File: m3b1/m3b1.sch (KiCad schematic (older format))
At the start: 26 parts, among them P5 MicroD-37Pins, Q1 MD3251, Q2 MD3251, U1 MC307, U10 MC309, U11 MC309, U12 MC310, U13 MC309, U2 MC306, U3 MC306, U4 MC306, U5 MC302, U6 MC306, U7 MC306, U8 MC301, U9 MC301

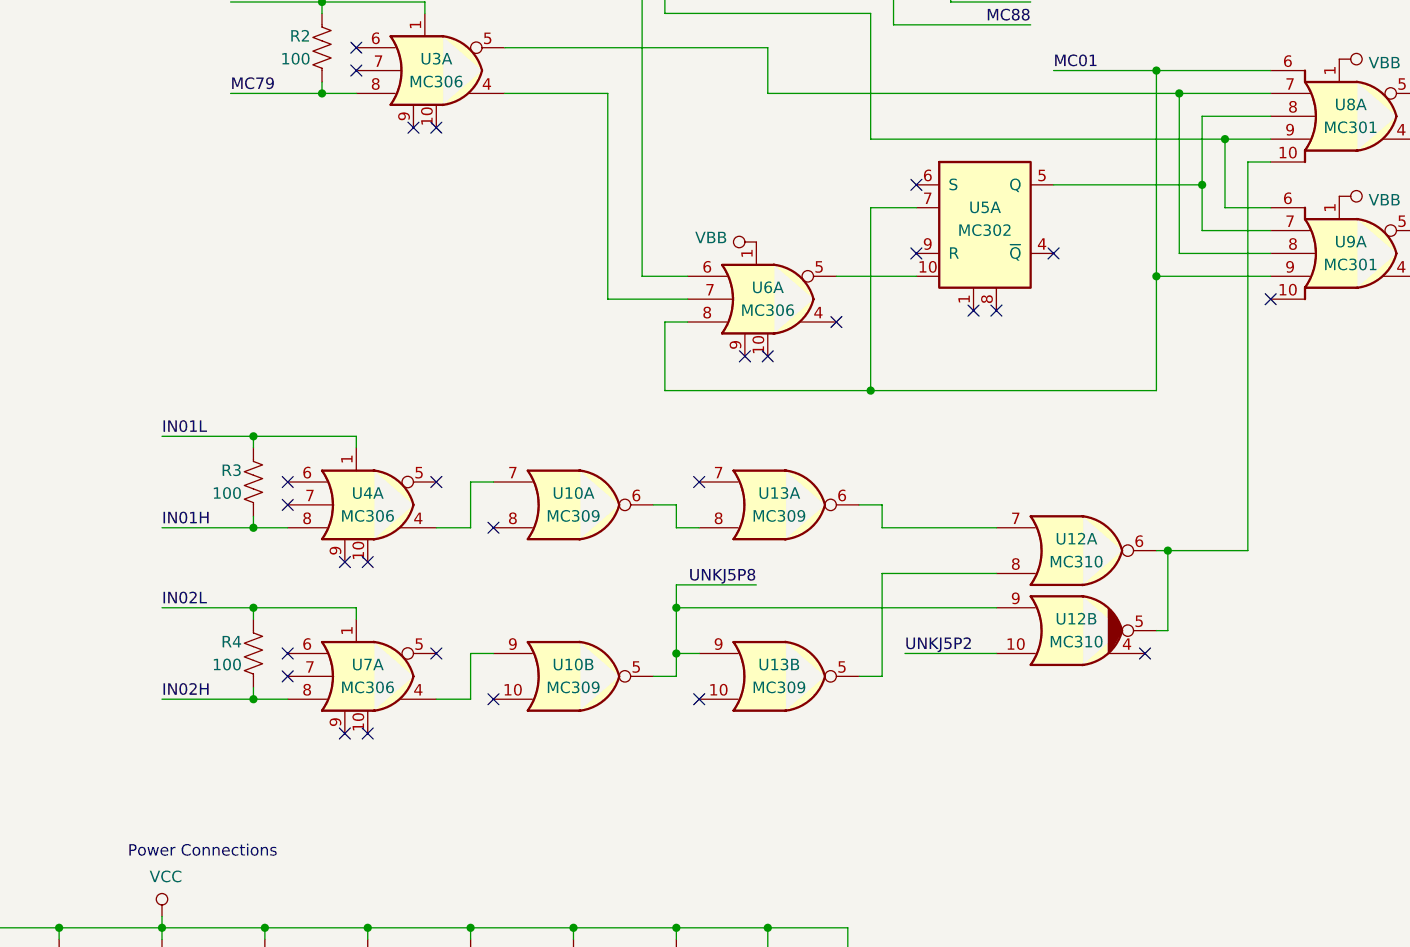
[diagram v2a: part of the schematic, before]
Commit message: Corrected a schematic error in module 3 board 1, which now makes much more sense. Also renamed the power good net to VFAIL.
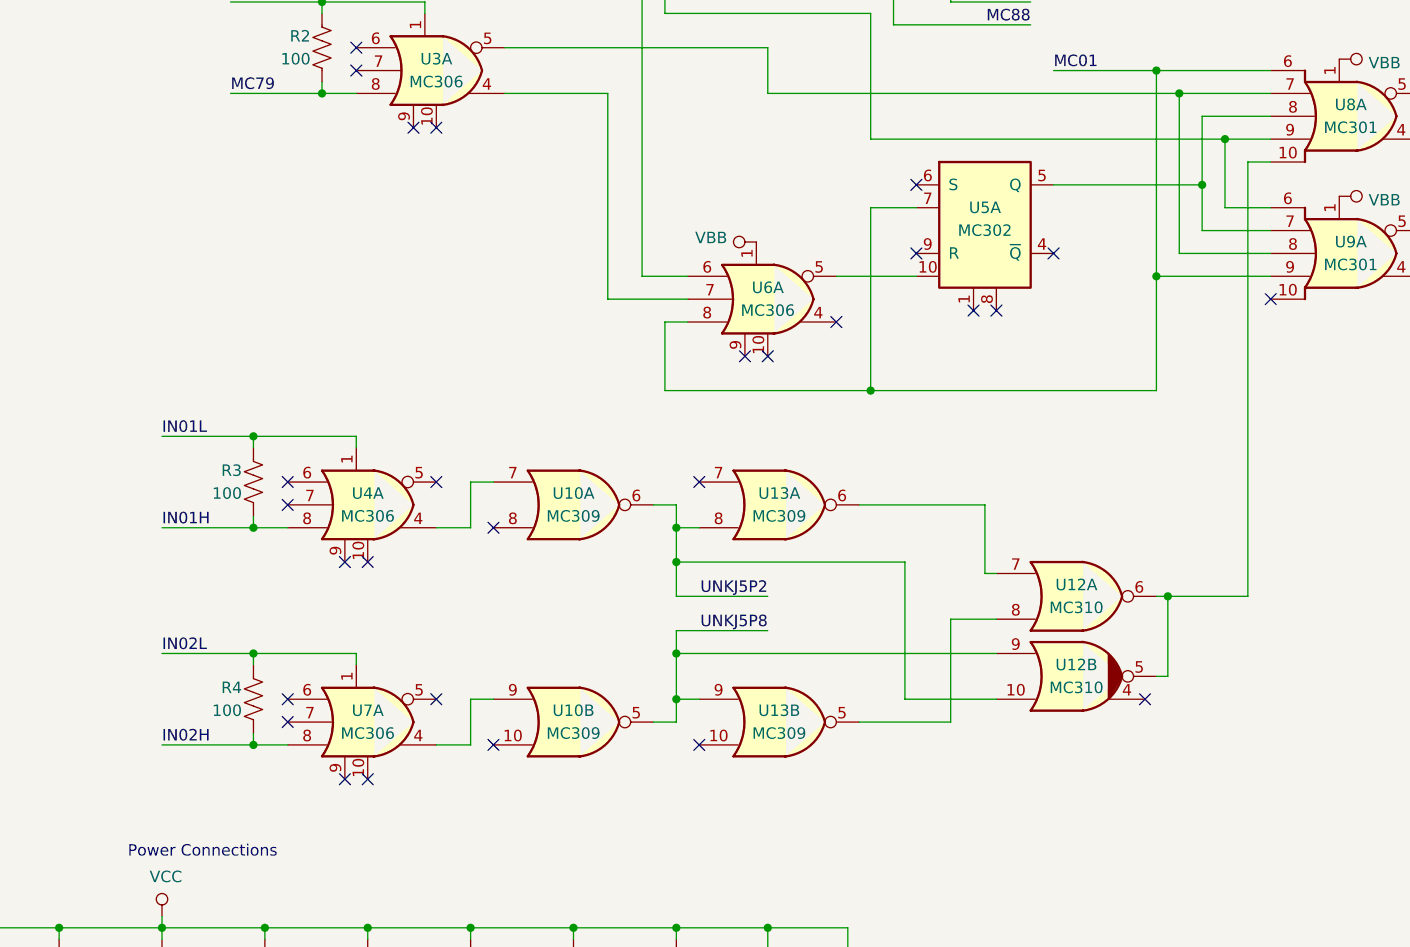
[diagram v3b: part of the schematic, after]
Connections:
- net UNKJ5P2: now also U10.6, U13.8
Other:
- moved on the sheet: R4, U10B, U12A, U12B, U13B, U7A
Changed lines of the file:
@@
 MC88
-$Comp
-L gn_buffer:MC306 U7
-U 1 1 5E8B1411
-P 4450 5100
-F 0 "U7" H 4400 5150 50  0000 C CNN
-F 1 "MC306" H 4400 5050 50  0000 C CNN
-F 2 "" H 4450 5100 50  0001 C CNN
-F 3 "http://www.ti.com/lit/gpn/sn74LS27" H 4450 5100 50  0001 C CNN
-	1    4450 5100
-	1    0    0    -1
-$EndComp
-NoConn ~ 4050 5000
-NoConn ~ 4050 5100
-$Comp
-L Device:R_US R4
-U 1 1 5E8B141D
-P 3900 5000
-F 0 "R4" H 3850 5050 50  0000 R CNN
-F 1 "100" H 3850 4950 50  0000 R CNN
-F 2 "" V 3940 4990 50  0001 C CNN
-F 3 "~" H 3900 5000 50  0001 C CNN
-	1    3900 5000
-	1    0    0    -1
-$EndComp
-Wire Wire Line
-	4050 5200 3900 5200
-Wire Wire Line
-	3900 5200 3900 5150
-Wire Wire Line
-	3900 4850 3900 4800
-Wire Wire Line
-	3900 4800 4350 4800
-Wire Wire Line
-	4350 4800 4350 4850
-NoConn ~ 4300 5350
-NoConn ~ 4400 5350
-Wire Wire Line
-	3900 5200 3500 5200
-Connection ~ 3900 5200
-Text Label 3500 5200 0    50   ~ 0
-IN02H
-Wire Wire Line
-	3900 4800 3500 4800
-Connection ~ 3900 4800
-Text Label 3500 4800 0    50   ~ 0
-IN02L
-NoConn ~ 4700 5000
 $Comp
 L gn_buffer:MC306 U6
@@
 	1    0    0    -1
 $EndComp
-$Comp
-L gn_buffer:MC309 U10
-U 2 1 5E8CFA6B
-P 5350 5100
-F 0 "U10" H 5300 5150 50  0000 C CNN
-F 1 "MC309" H 5300 5050 50  0000 C CNN
-F 2 "" H 5350 5100 50  0001 C CNN
-F 3 "http://www.ti.com/lit/gpn/sn74LS27" H 5350 5100 50  0001 C CNN
-	2    5350 5100
-	1    0    0    -1
-$EndComp
 Wire Wire Line
 	4700 4450 4850 4450
@@
 	4850 4250 4950 4250
 NoConn ~ 4950 4450
-Wire Wire Line
-	4700 5200 4850 5200
-Wire Wire Line
-	4850 5200 4850 5000
-Wire Wire Line
-	4850 5000 4950 5000
-NoConn ~ 4950 5200
 $Comp
 L gn_buffer:MC309 U13
@@
 	1    0    0    -1
 $EndComp
-$Comp
-L gn_buffer:MC309 U13
-U 2 1 5E8EC42C
-P 6250 5100
-F 0 "U13" H 6200 5150 50  0000 C CNN
-F 1 "MC309" H 6200 5050 50  0000 C CNN
-F 2 "" H 6250 5100 50  0001 C CNN
-F 3 "http://www.ti.com/lit/gpn/sn74LS27" H 6250 5100 50  0001 C CNN
-	2    6250 5100
-	1    0    0    -1
-$EndComp
-Wire Wire Line
-	5650 5100 5750 5100
-Wire Wire Line
-	5750 5100 5750 5000
-Wire Wire Line
-	5750 5000 5850 5000
 Wire Wire Line
 	5650 4350 5750 4350
@@
 Wire Wire Line
 	5750 4450 5850 4450
-Wire Wire Line
-	5750 5000 5750 4800
-Wire Wire Line
-	5750 4800 7150 4800
-Connection ~ 5750 5000
-Text Label 6100 4700 2    50   ~ 0
-UNKJ5P8
 NoConn ~ 5850 4250
-NoConn ~ 5850 5200
 $Comp
 L gn_buffer:MC310 U12
 U 1 1 5E90B666
-P 7550 4550
-F 0 "U12" H 7500 4600 50  0000 C CNN
-F 1 "MC310" H 7500 4500 50  0000 C CNN
-F 2 "" H 7550 4550 50  0001 C CNN
-F 3 "http://www.ti.com/lit/gpn/sn74LS27" H 7550 4550 50  0001 C CNN
-	1    7550 4550
+P 7550 4750
+F 0 "U12" H 7500 4800 50  0000 C CNN
+F 1 "MC310" H 7500 4700 50  0000 C CNN
+F 2 "" H 7550 4750 50  0001 C CNN
+F 3 "http://www.ti.com/lit/gpn/sn74LS27" H 7550 4750 50  0001 C CNN
+	1    7550 4750
 	1    0    0    -1
 $EndComp
@@
 L gn_buffer:MC310 U12
 U 2 1 5E90D3C4
-P 7550 4900
-F 0 "U12" H 7500 4950 50  0000 C CNN
-F 1 "MC310" H 7500 4850 50  0000 C CNN
-F 2 "" H 7550 4900 50  0001 C CNN
-F 3 "http://www.ti.com/lit/gpn/sn74LS27" H 7550 4900 50  0001 C CNN
-	2    7550 4900
-	1    0    0    -1
-$EndComp
-NoConn ~ 7800 5000
-Wire Wire Line
-	7850 4550 7900 4550
-Wire Wire Line
-	7900 4550 7900 4900
-Wire Wire Line
-	7900 4900 7850 4900
-Wire Wire Line
-	7150 5000 6750 5000
-Text Label 6750 5000 0    50   ~ 0
-UNKJ5P2
-Wire Wire Line
-	6100 4700 5750 4700
-Wire Wire Line
-	5750 4700 5750 4800
-Connection ~ 5750 4800
-Wire Wire Line
-	7150 4650 6650 4650
-Wire Wire Line
-	6650 4650 6650 5100
-Wire Wire Line
-	6650 5100 6550 5100
-Wire Wire Line
-	6550 4350 6650 4350
-Wire Wire Line
-	6650 4350 6650 4450
-Wire Wire Line
-	6650 4450 7150 4450
-Wire Wire Line
-	7900 4550 8250 4550
-Wire Wire Line
-	8250 4550 8250 2850
+P 7550 5100
+F 0 "U12" H 7500 5150 50  0000 C CNN
+F 1 "MC310" H 7500 5050 50  0000 C CNN
+F 2 "" H 7550 5100 50  0001 C CNN
+F 3 "http://www.ti.com/lit/gpn/sn74LS27" H 7550 5100 50  0001 C CNN
+	2    7550 5100
+	1    0    0    -1
+$EndComp
+NoConn ~ 7800 5200
+Wire Wire Line
+	7850 4750 7900 4750
+Wire Wire Line
+	7900 4750 7900 5100
+Wire Wire Line
+	7900 5100 7850 5100
+Wire Wire Line
+	7150 4850 6950 4850
+Wire Wire Line
+	6550 4350 7100 4350
+Wire Wire Line
+	7100 4350 7100 4650
+Wire Wire Line
+	7100 4650 7150 4650
+Wire Wire Line
+	7900 4750 8250 4750
+Wire Wire Line
+	8250 4750 8250 2850
 Wire Wire Line
 	8250 2850 8350 2850
-Connection ~ 7900 4550
+Connection ~ 7900 4750
 $Comp
 L gn_buffer:MC309 U11
@@
 Text Notes 3350 5900 0    50   ~ 0
 Power Connections
+NoConn ~ 4300 5550
+NoConn ~ 4400 5550
+Wire Wire Line
+	6950 5300 6550 5300
+Wire Wire Line
+	6950 4850 6950 5300
+Connection ~ 5750 5000
+Wire Wire Line
+	5750 4900 5750 5000
+Wire Wire Line
+	6150 4900 5750 4900
+Text Label 6150 4750 2    50   ~ 0
+UNKJ5P2
+Wire Wire Line
+	5750 4750 6150 4750
+NoConn ~ 5850 5400
+Text Label 6150 4900 2    50   ~ 0
+UNKJ5P8
+Connection ~ 5750 5200
+Wire Wire Line
+	5750 5000 7150 5000
+Wire Wire Line
+	5750 5200 5750 5000
+Wire Wire Line
+	5750 5200 5850 5200
+Wire Wire Line
+	5750 5300 5750 5200
+Wire Wire Line
+	5650 5300 5750 5300
+$Comp
+L gn_buffer:MC309 U13
+U 2 1 5E8EC42C
+P 6250 5300
+F 0 "U13" H 6200 5350 50  0000 C CNN
+F 1 "MC309" H 6200 5250 50  0000 C CNN
+F 2 "" H 6250 5300 50  0001 C CNN
+F 3 "http://www.ti.com/lit/gpn/sn74LS27" H 6250 5300 50  0001 C CNN
+	2    6250 5300
+	1    0    0    -1
+$EndComp
+NoConn ~ 4950 5400
+Wire Wire Line
+	4850 5200 4950 5200
+Wire Wire Line
+	4850 5400 4850 5200
+Wire Wire Line
+	4700 5400 4850 5400
+$Comp
+L gn_buffer:MC309 U10
+U 2 1 5E8CFA6B
+P 5350 5300
+F 0 "U10" H 5300 5350 50  0000 C CNN
+F 1 "MC309" H 5300 5250 50  0000 C CNN
+F 2 "" H 5350 5300 50  0001 C CNN
+F 3 "http://www.ti.com/lit/gpn/sn74LS27" H 5350 5300 50  0001 C CNN
+	2    5350 5300
+	1    0    0    -1
+$EndComp
+NoConn ~ 4700 5200
+Text Label 3500 5000 0    50   ~ 0
+IN02L
+Connection ~ 3900 5000
+Wire Wire Line
+	3900 5000 3500 5000
+Text Label 3500 5400 0    50   ~ 0
+IN02H
+Connection ~ 3900 5400
+Wire Wire Line
+	3900 5400 3500 5400
+Wire Wire Line
+	4350 5000 4350 5050
+Wire Wire Line
+	3900 5000 4350 5000
+Wire Wire Line
+	3900 5050 3900 5000
+Wire Wire Line
+	3900 5400 3900 5350
+Wire Wire Line
+	4050 5400 3900 5400
+$Comp
+L Device:R_US R4
+U 1 1 5E8B141D
+P 3900 5200
+F 0 "R4" H 3850 5250 50  0000 R CNN
+F 1 "100" H 3850 5150 50  0000 R CNN
+F 2 "" V 3940 5190 50  0001 C CNN
+F 3 "~" H 3900 5200 50  0001 C CNN
+	1    3900 5200
+	1    0    0    -1
+$EndComp
+NoConn ~ 4050 5300
+NoConn ~ 4050 5200
+$Comp
+L gn_buffer:MC306 U7
+U 1 1 5E8B1411
+P 4450 5300
+F 0 "U7" H 4400 5350 50  0000 C CNN
+F 1 "MC306" H 4400 5250 50  0000 C CNN
+F 2 "" H 4450 5300 50  0001 C CNN
+F 3 "http://www.ti.com/lit/gpn/sn74LS27" H 4450 5300 50  0001 C CNN
+	1    4450 5300
+	1    0    0    -1
+$EndComp
+Wire Wire Line
+	5750 4450 5750 4600
+Connection ~ 5750 4450
+Wire Wire Line
+	5750 4600 6750 4600
+Wire Wire Line
+	6750 4600 6750 5200
+Wire Wire Line
+	6750 5200 7150 5200
+Connection ~ 5750 4600
+Wire Wire Line
+	5750 4600 5750 4750
 $EndSCHEMATC

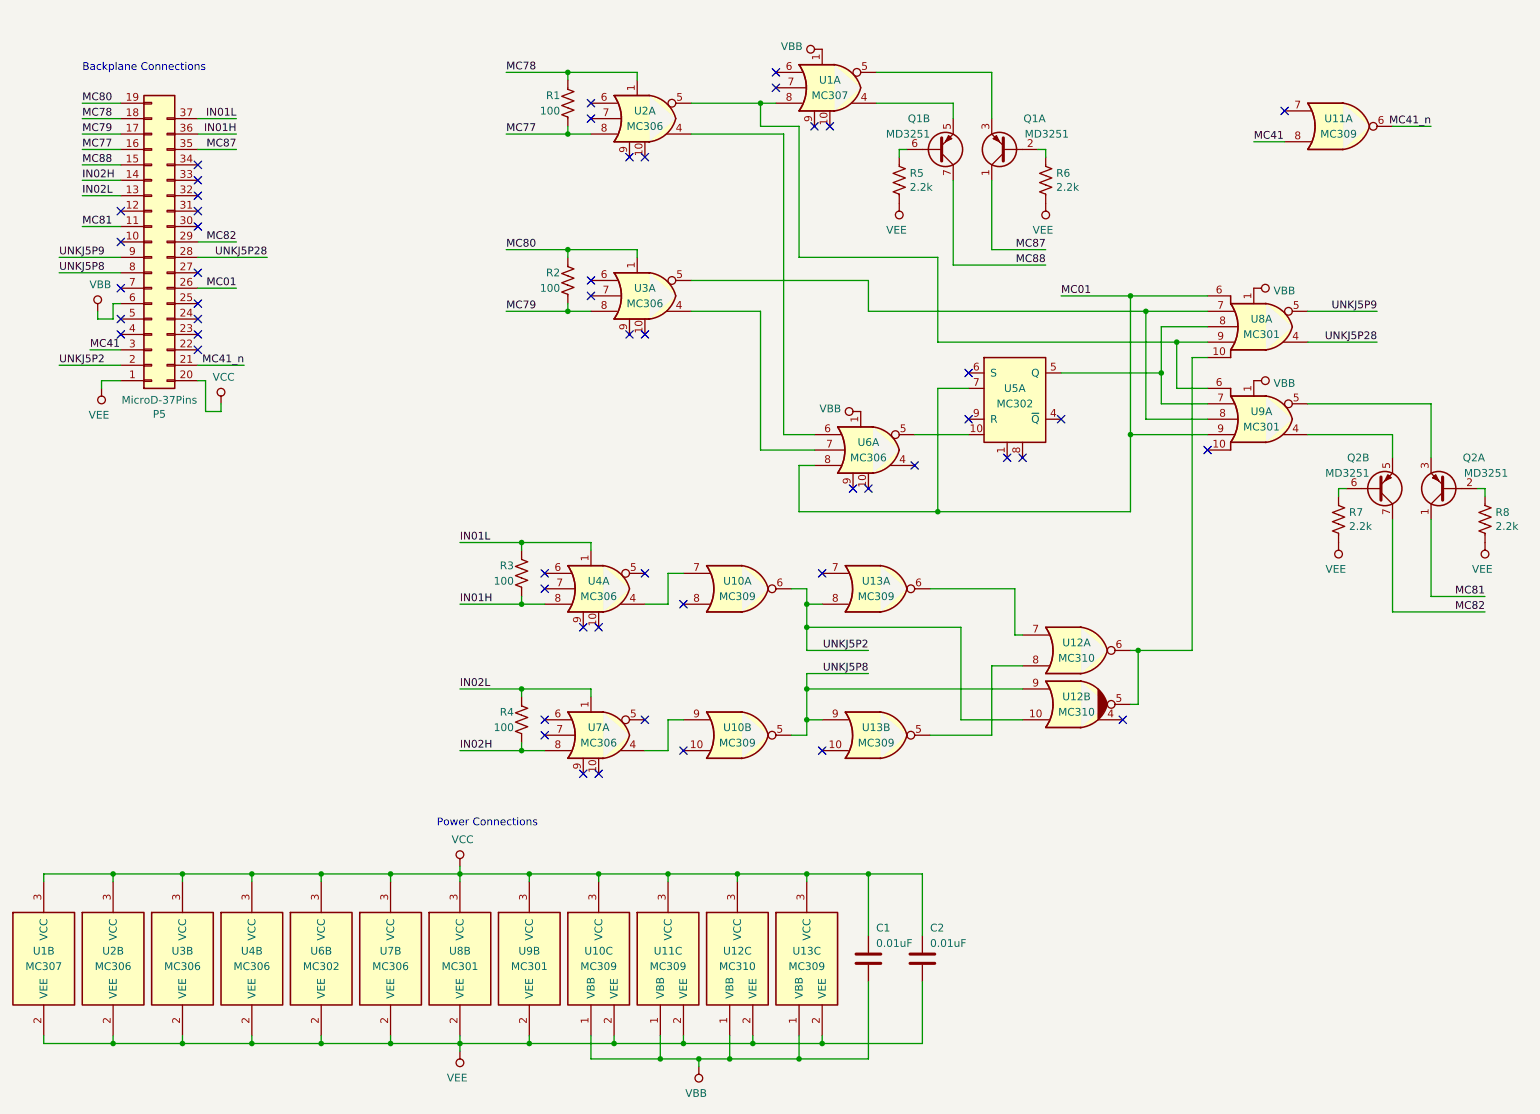
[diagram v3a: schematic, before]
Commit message: Some work on reorganizing the module 3 schematics
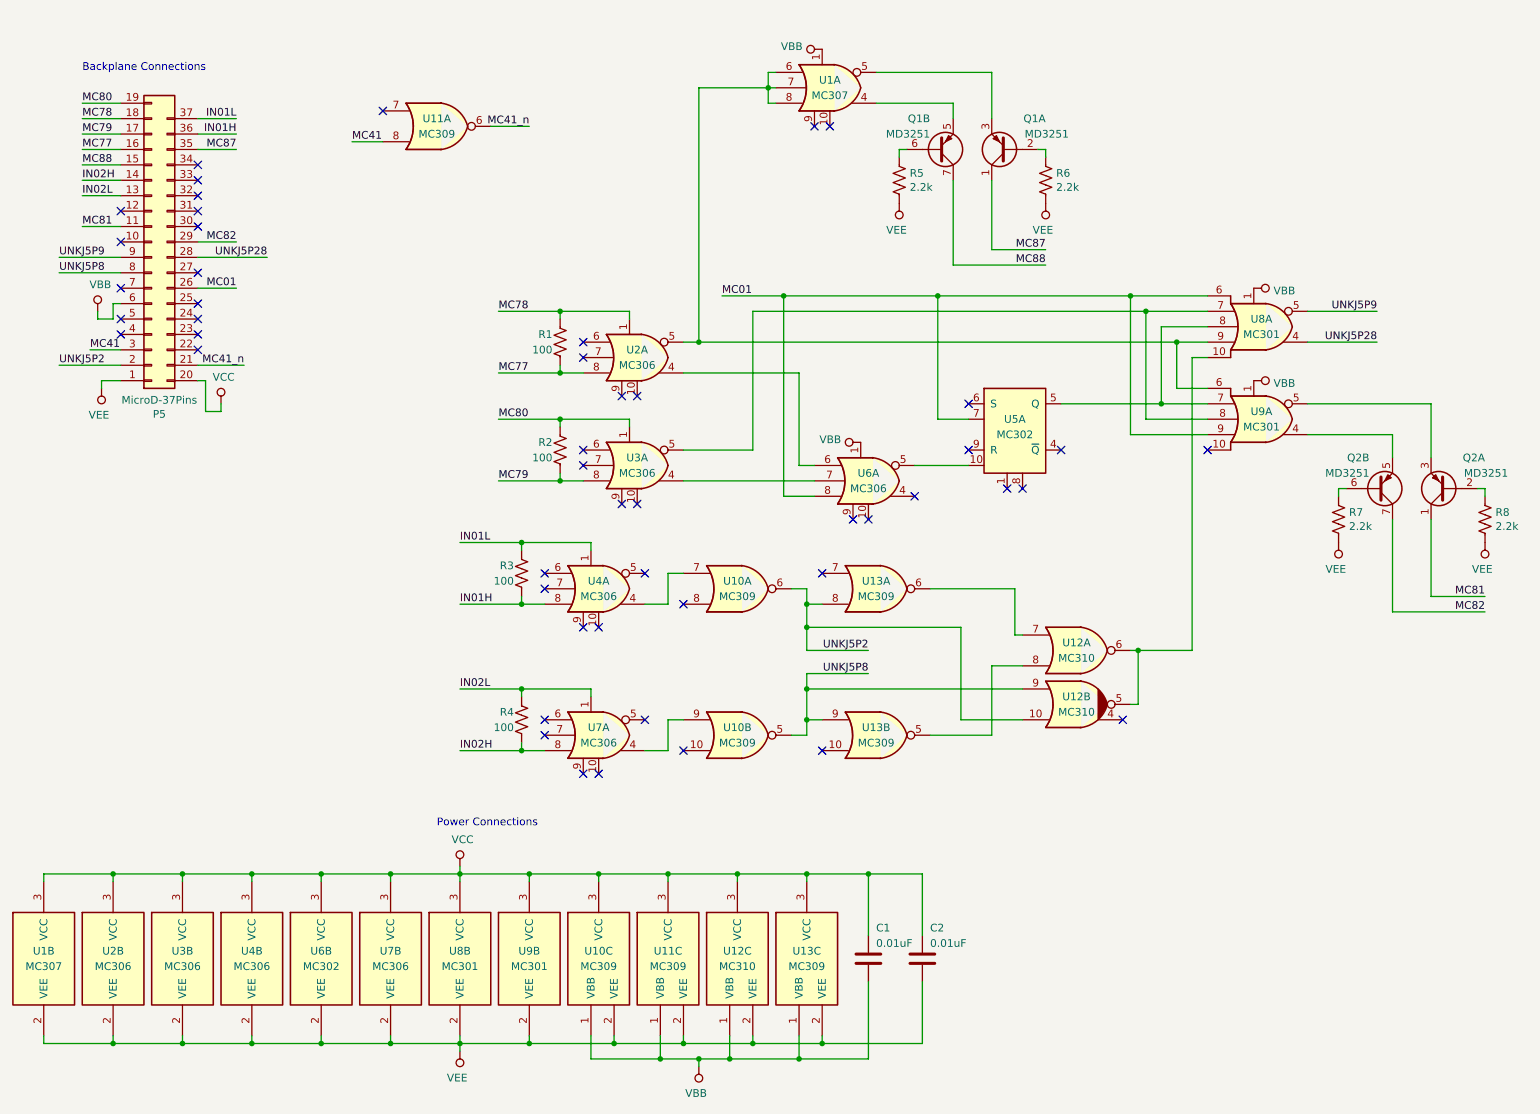
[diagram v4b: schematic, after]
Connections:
- net at U1.8, U2.5, U8.9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: now also U1.6, U1.7
- no-connect marks 52 -> 50
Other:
- moved on the sheet: R1, R2, U11A, U2A, U3A, U5A, U6A
